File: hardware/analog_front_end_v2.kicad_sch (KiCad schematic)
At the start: 101 parts, among them J1 Conn_Coaxial, J3 Conn_01x01_Socket, J4 Conn_01x01_Socket, U1 ADL5531, U10 MAX6002, U11 LP2985-5.0, U12 MAX2606, U13 PAT1220-C-0DB, U14 LP2985-5.0, U15 BFP540ESD, U16 BFP540ESD, U17 LP2985-3.3, U18 PAT1220-C-0DB, U19 PAT1220-C-0DB, U2 ADL5531, U20 PAT1220-C-0DB, U21 PAT1220-C-0DB, U3 ADL5531, U4 ADL5531, U5 LP2985-1.8, U6 MCP33131, U7 PAT1220-C-0DB, U8 ADL5531, U9 PMOD 2x6

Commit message: Updated KiCAD prj/sch/pcb files that were sent for manufacturing
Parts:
- U13, U18, U19, U20, U21, U7: MPN (none) -> PAT1220-C-5DB-T5
- U17: MPN (none) -> LP2985-33DBVR
- U6: footprint Package_SO:MSOP-10_3x3mm_P0.5mm -> TheEEView_Footprint_Lib:MCP33131; MOC MCP33131-10-E/MS -> MCP33131-05-E/MS-ND
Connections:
- net ADC_VREF renamed ADC_VREF_2V5
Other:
- note added: "Cascode based mixer for 86MHz to 106MHz band"
- note added: "Input range 0 to 2.6V (Vref+0.1)"
- note removed: "Cascode based mixer for 96MHz to 106MHz band"

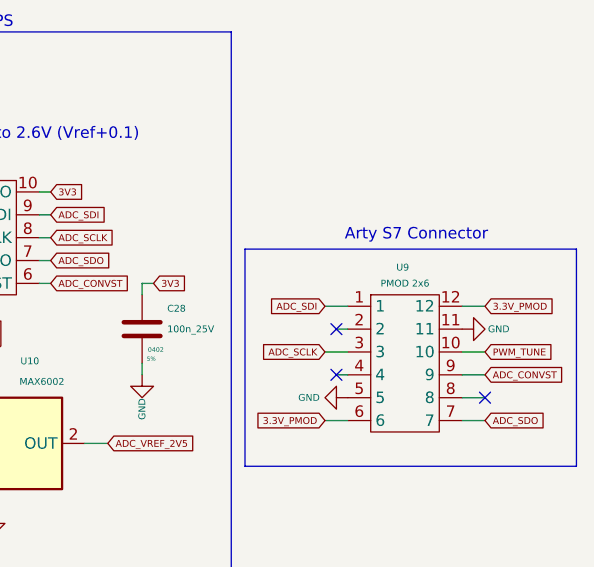
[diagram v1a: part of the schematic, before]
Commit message: Updated KiCAD Prj,sch,pcb files for 2.54mm PMOD male connector
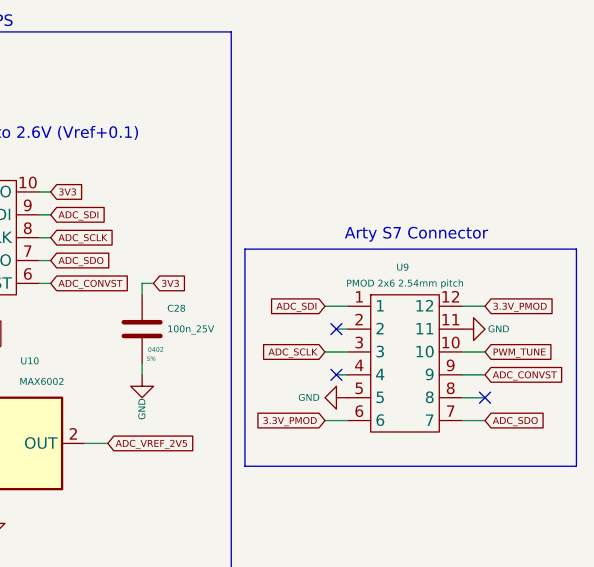
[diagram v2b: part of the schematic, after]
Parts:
- U9: value PMOD 2x6 -> PMOD 2x6 2.54mm pitch; footprint Connector_PinHeader_1.00mm:PinHeader_2x06_P1.00mm_Vertical -> Connector_PinHeader_2.54mm:PinHeader_2x06_P2.54mm_Vertical
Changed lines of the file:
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@@
 			)
 		)
-		(property "Value" "PMOD 2x6"
+		(property "Value" "PMOD 2x6 2.54mm pitch"
 			(at 509.27 54.61 0)
 			(effects
@@
 			)
 		)
-		(property "Footprint" "Connector_PinHeader_1.00mm:PinHeader_2x06_P1.00mm_Vertical"
+		(property "Footprint" "Connector_PinHeader_2.54mm:PinHeader_2x06_P2.54mm_Vertical"
 			(at 509.27 60.96 0)
 			(effects

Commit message: Update prj/sch/pcb files sent off for manufacturing
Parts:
- added C53: 10n_25V, Capacitor_SMD:C_0402_1005Metric, symbol Device:C
- added C54: 100n_25V, Capacitor_SMD:C_0402_1005Metric, symbol Device:C
- added R2: 100, Resistor_SMD:R_0402_1005Metric, symbol Device:R
- added U22: MCP6286, Package_TO_SOT_SMD:SOT-23-5, symbol TheEEView_Global_Lib:MCP6286
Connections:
- net 3V3: now also C54.1, U22.5 (Vdd)
- net GND: now also C53.2, C54.2, U22.2 (Vss)
- net at R10.2, U15.3 (C): now also U22.3 (Vin+); no longer C26.1
- new net: R2.1, U22.1 (Vout), U22.4 (Vin-)
- new net: C26.1, C53.1, R2.2
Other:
- note added: "320kHz anti-aliasing filter"
- note added: "DC shift for ADC"
- moved on the sheet: C26, C27, C28, C52, L6, R3, U10, U6, U9
